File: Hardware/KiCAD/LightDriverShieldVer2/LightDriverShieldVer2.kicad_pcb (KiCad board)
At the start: 4 copper layers, 25.5 x 49.5 mm, 24 parts, among them J1 Conn_01x12, J2 Conn_01x12, J3 Conn_01x06, J4 Screw_Terminal_01x04, J5 ExtVCC, Q1 MMBT3904, Q2 Si2301, Q3 MMBT3904, Q4 MMBT3904, Q5 MMBT3904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

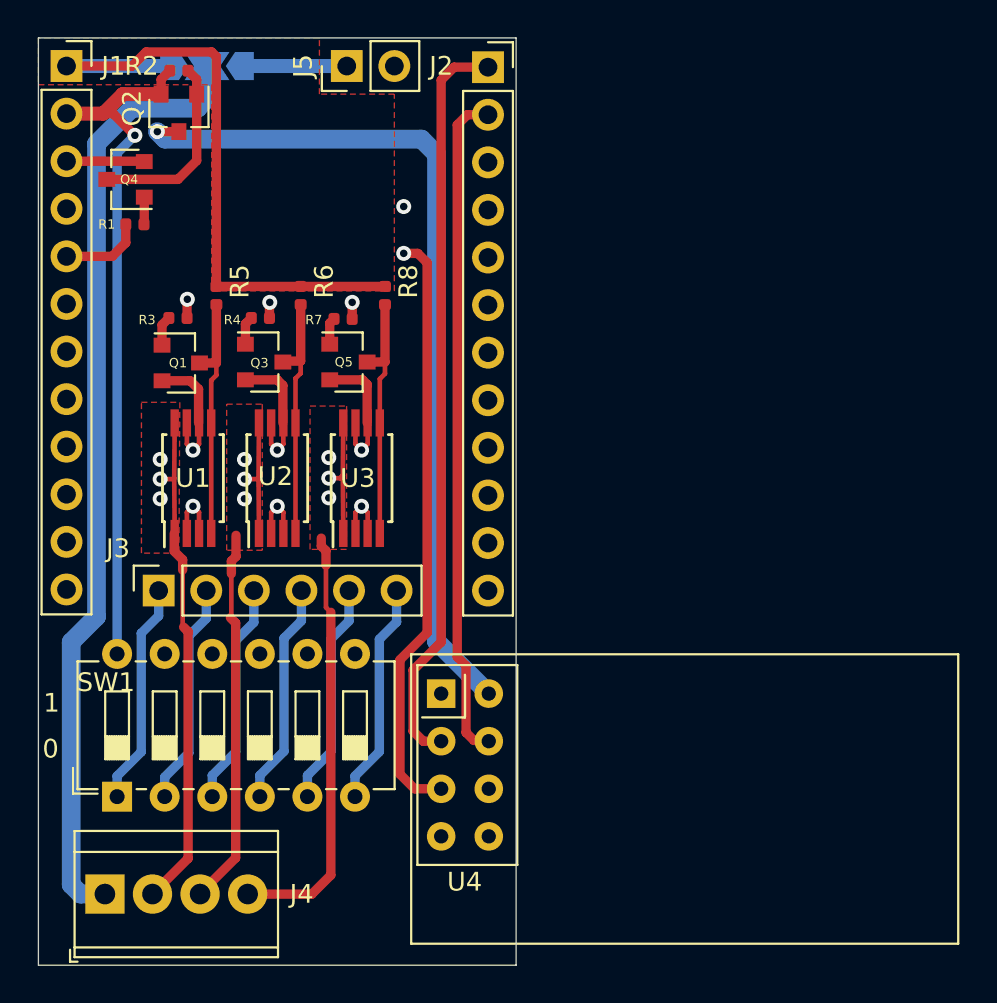
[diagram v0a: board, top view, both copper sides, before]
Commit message: Swapped MMBT3904 BJTs to SI2302 NMOS. Fixes bug where the B-E junction forces the GPIO pin controlling ON/OFF state to be clamped at ~0.6v.
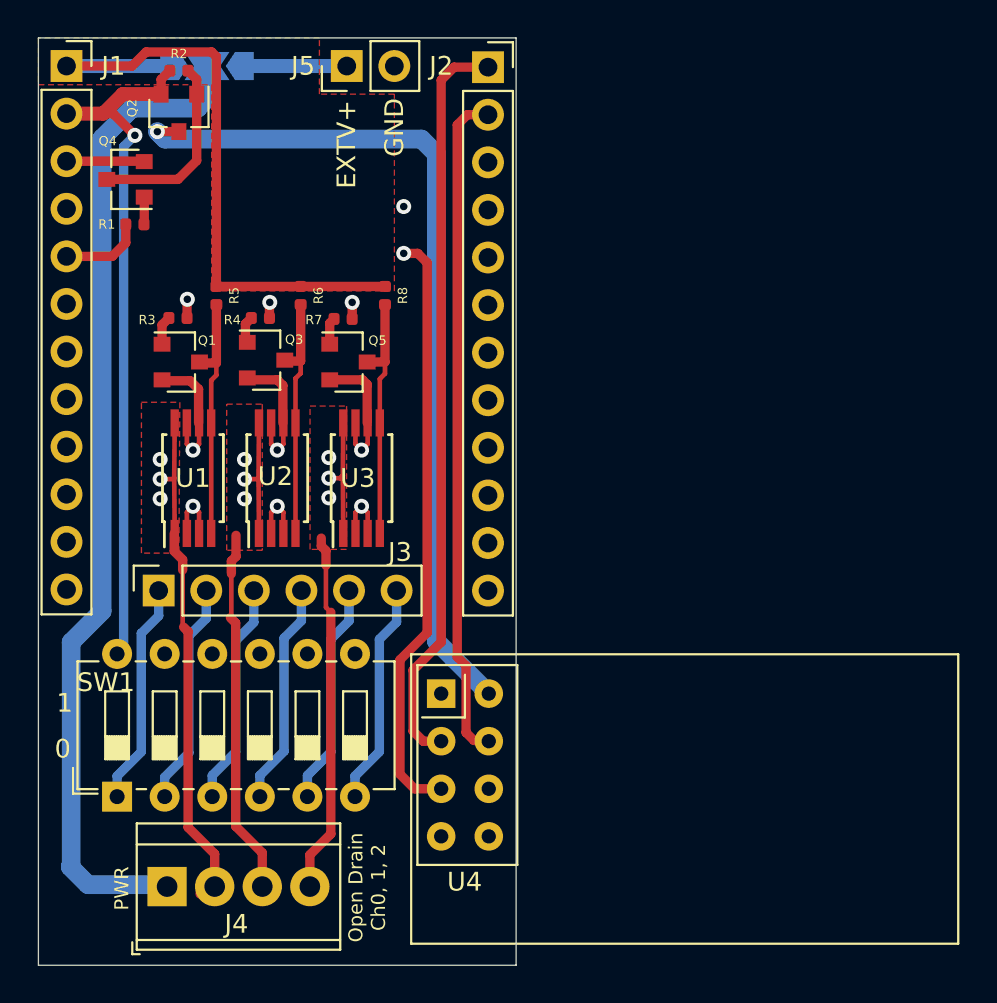
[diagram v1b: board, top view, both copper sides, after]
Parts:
- Q1, Q3, Q4, Q5: value MMBT3904 -> Si2302
- moved J4 3.34 mm to (105.4, 135.8)
- moved Q3 0.14 mm to (110.7, 107.7)
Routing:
- net DRV2: track 29.8 -> 26.0 mm
- net VCCO: track 50.8 -> 53.4 mm
- net DRV1: track 27.3 -> 26.7 mm
- net DRV0: track 27.0 -> 26.4 mm
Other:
- board text added: "+5V"
- board text added: "EXTV+"
- board text added: "GND"
- board text added: "Networked PWM Driver Version 2.1 Brandon Braun 7/22/2020"
- board text added: "Open Drain Ch0, 1, 2"
- board text added: "PWR"
- board text removed: "EXT_+5V"
- board text removed: "INT_+5V"
